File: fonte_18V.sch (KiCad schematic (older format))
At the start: 27 parts, among them U1 LMR16030

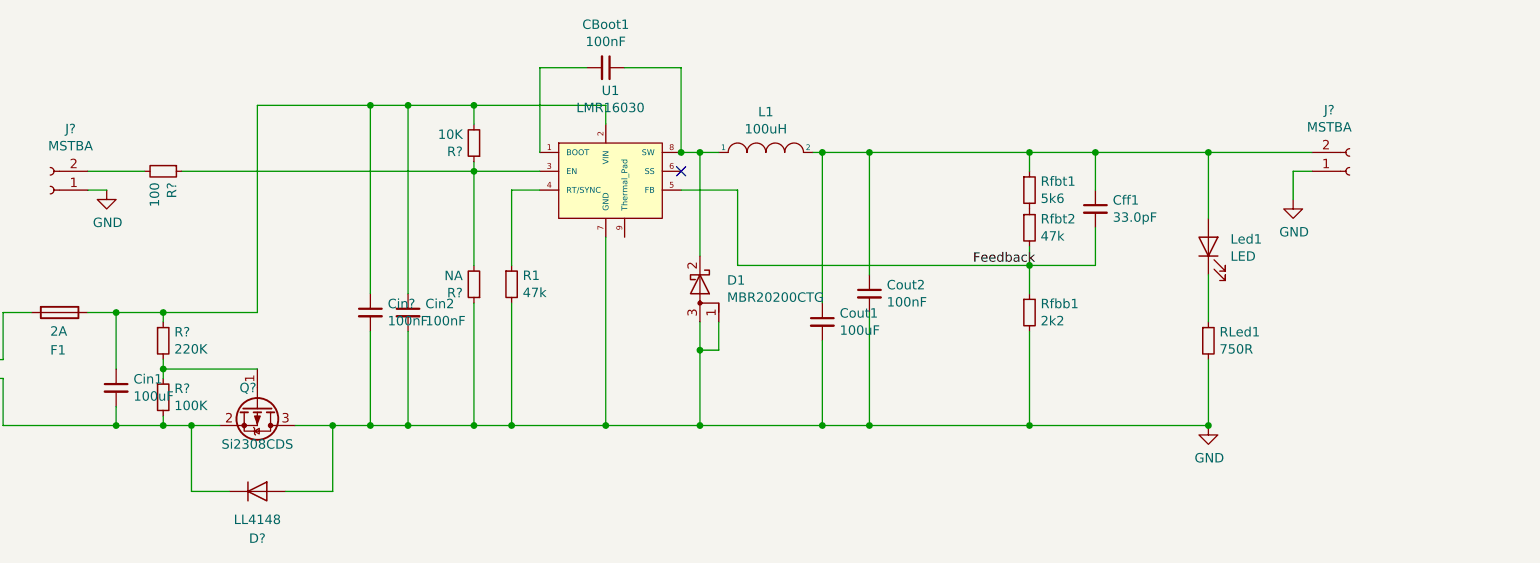
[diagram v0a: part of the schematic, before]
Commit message: snuber e capacitores adicionados. valores de capacitores alterados
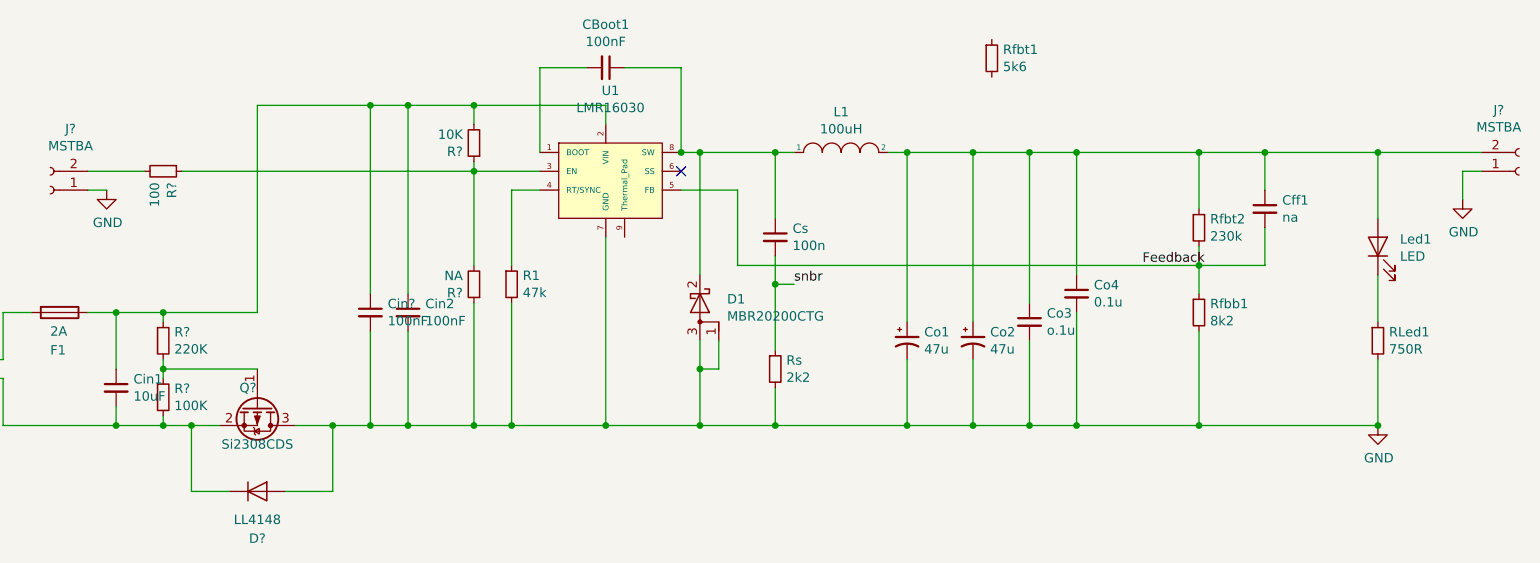
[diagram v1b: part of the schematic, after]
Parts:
- added Co1, Co2: 47u, symbol Device:CP1_Small
- added Cs: 100n, Capacitor_THT:CP_Radial_D8.0mm_P3.80mm, symbol fonte_18V-rescue:C_Small-Device
- added Rs: 2k2, Resistor_SMD:R_0805_2012Metric_Pad1.15x1.40mm_HandSolder, symbol fonte_18V-rescue:R_Small-Device
- Cff1: value 33.0pF -> na
- Cin1: value 100uF -> 10uF
- Co3: renamed from Cout1; value 100uF -> o.1u
- Co4: renamed from Cout2; value 100nF -> 0.1u
- Rfbb1: value 2k2 -> 8k2
- Rfbt2: value 47k -> 230k
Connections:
- net GND: now also Co1.2, Co2.2, Rs.2
- net at CBoot1.1, D1.2 (K), L1.1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: now also Cs.1
- net at Cff1.1, Co3.1, Co4.1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: now also Rfbt2.1, Co1.1, Co2.1; no longer Rfbt1.1
- net at Rfbt1.2: no longer Rfbt2.1
- new net snbr: Cs.2, Rs.1
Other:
- moved on the sheet: Cff1, Co3, Co4, D1, J?, L1, Led1, RLed1, Rfbb1, Rfbt1, Rfbt2

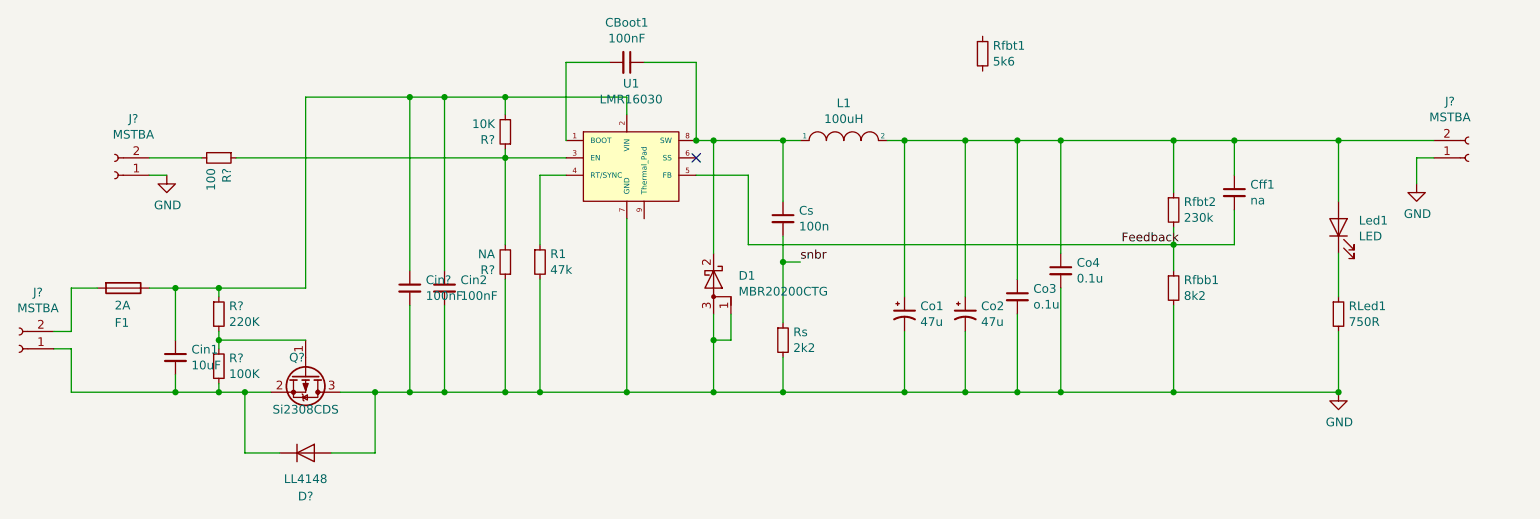
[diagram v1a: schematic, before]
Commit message: mudança de capacitores de entrada nomeou os componentes do circuito footprints alterados erc rodado
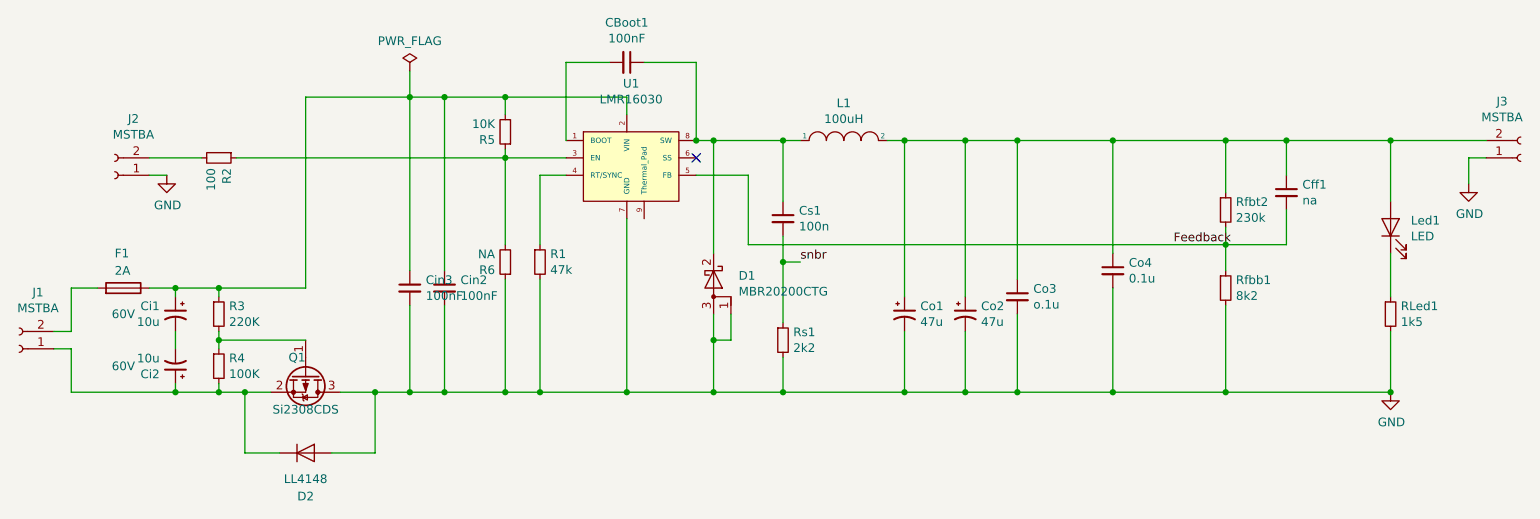
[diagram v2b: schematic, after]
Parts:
- removed Cin1: 10uF, Capacitor_THT:CP_Radial_D8.0mm_P3.80mm, symbol fonte_18V-rescue:C_Small-Device
- removed Rfbt1: 5k6, Resistor_SMD:R_0805_2012Metric_Pad1.15x1.40mm_HandSolder, symbol fonte_18V-rescue:R_Small-Device
- added Ci1, Ci2: 10u, Capacitor_THT:CP_Radial_D5.0mm_P2.50mm, symbol Device:CP1_Small
- Co1, Co2: footprint (none) -> Capacitor_THT:CP_Radial_D5.0mm_P2.50mm
- Co3: footprint Capacitor_THT:CP_Radial_D8.0mm_P3.80mm -> Capacitor_SMD:C_0805_2012Metric_Pad1.15x1.40mm_HandSolder
- Cs1: renamed from Cs; footprint Capacitor_THT:CP_Radial_D8.0mm_P3.80mm -> Capacitor_SMD:C_0805_2012Metric_Pad1.15x1.40mm_HandSolder
- RLed1: value 750R -> 1k5
- gave numbers to parts that had none: 11
- renumbered Rs to Rs1
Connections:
- net at Cin2.1, Cin3.1, F1.1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: now also Ci1.1
- net at D2.1 (K), J1.1 (Pin_1), Q1.2 (S)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: now also Ci2.1
- new net: Ci1.2, Ci2.2
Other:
- moved on the sheet: Cff1, Co4, J3, Led1, RLed1, Rfbb1, Rfbt2

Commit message: Conectores rj45 adicionados, trilhas melhoradas, acabamentos gerais
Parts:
- removed D2: LL4148, Diode_SMD:D_MiniMELF, symbol Diode:LL4148
- removed J3: MSTBA, Connector_Phoenix_MSTB:PhoenixContact_MSTBA_2,5_2-G-5,08_1x02_P5.08mm_Horizontal, symbol Connector:Conn_01x02_Female
- added H1, H2, H3, H4: MountingHole, MountingHole:MountingHole_3.2mm_M3, symbol Mechanical:MountingHole
- added J3, J4: RJ45_Shielded, MFP19RJ45:RJ45_YH59_01, symbol Connector:RJ45_Shielded
- Q1: symbol Transistor_FET:Si2319CDS -> Device:Q_NMOS_GSD
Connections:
- net GND: now also Q1.2 (S), R4.2, U1.9 (Thermal_Pad), J3.3, J3.6, J3.7, J3.8, J3.SH, J4.3, J4.6, J4.7, J4.8, J4.SH; no longer Q1.3 (D)
- net CAN_18V: now reaches Cff1.1, Co1.1, Co2.1, Co3.1, Co4.1, L1.2, Led1.2 (A), Rfbt2.1
- net CAN_18V: now also J3.4, J3.5, J4.4, J4.5
- net at Ci2.1, J1.1 (Pin_1): now also Q1.3 (D); no longer Q1.2 (S), R4.2
- no-connect marks 1 -> 5
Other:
- moved on the sheet: CBoot1, Cff1, Ci1, Ci2, Cin2, Cin3, Co1, Co2, Co3, Co4, Cs1, D1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

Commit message: atualizado
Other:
- moved on the sheet: H1, H2, H3, H4
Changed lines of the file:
@@
 L Mechanical:MountingHole H4
 U 1 1 5DB5A7FD
-P 11550 200
-F 0 "H4" H 11650 246 50  0000 L CNN
-F 1 "MountingHole" H 11650 155 50  0000 L CNN
-F 2 "MountingHole:MountingHole_3.2mm_M3" H 11550 200 50  0001 C CNN
-F 3 "~" H 11550 200 50  0001 C CNN
-	1    11550 200
+P 3250 2200
+F 0 "H4" H 3350 2246 50  0000 L CNN
+F 1 "MountingHole" H 3350 2155 50  0000 L CNN
+F 2 "MountingHole:MountingHole_3.2mm_M3" H 3250 2200 50  0001 C CNN
+F 3 "~" H 3250 2200 50  0001 C CNN
+	1    3250 2200
 	1    0    0    -1
 $EndComp
@@
 L Mechanical:MountingHole H3
 U 1 1 5DB774A1
-P 11500 8100
-F 0 "H3" H 11600 8146 50  0000 L CNN
-F 1 "MountingHole" H 11600 8055 50  0000 L CNN
-F 2 "MountingHole:MountingHole_3.2mm_M3" H 11500 8100 50  0001 C CNN
-F 3 "~" H 11500 8100 50  0001 C CNN
-	1    11500 8100
+P 3250 2550
+F 0 "H3" H 3350 2596 50  0000 L CNN
+F 1 "MountingHole" H 3350 2505 50  0000 L CNN
+F 2 "MountingHole:MountingHole_3.2mm_M3" H 3250 2550 50  0001 C CNN
+F 3 "~" H 3250 2550 50  0001 C CNN
+	1    3250 2550
 	1    0    0    -1
 $EndComp
@@
 L Mechanical:MountingHole H2
 U 1 1 5DB7A851
-P 200 8100
-F 0 "H2" H 300 8146 50  0000 L CNN
-F 1 "MountingHole" H 300 8055 50  0000 L CNN
-F 2 "MountingHole:MountingHole_3.2mm_M3" H 200 8100 50  0001 C CNN
-F 3 "~" H 200 8100 50  0001 C CNN
-	1    200  8100
+P 2350 2550
+F 0 "H2" H 2450 2596 50  0000 L CNN
+F 1 "MountingHole" H 2450 2505 50  0000 L CNN
+F 2 "MountingHole:MountingHole_3.2mm_M3" H 2350 2550 50  0001 C CNN
+F 3 "~" H 2350 2550 50  0001 C CNN
+	1    2350 2550
 	1    0    0    -1
 $EndComp
@@
 L Mechanical:MountingHole H1
 U 1 1 5DB7DBB6
-P 200 150
-F 0 "H1" H 300 196 50  0000 L CNN
-F 1 "MountingHole" H 300 105 50  0000 L CNN
-F 2 "MountingHole:MountingHole_3.2mm_M3" H 200 150 50  0001 C CNN
-F 3 "~" H 200 150 50  0001 C CNN
-	1    200  150
+P 2350 2200
+F 0 "H1" H 2450 2246 50  0000 L CNN
+F 1 "MountingHole" H 2450 2155 50  0000 L CNN
+F 2 "MountingHole:MountingHole_3.2mm_M3" H 2350 2200 50  0001 C CNN
+F 3 "~" H 2350 2200 50  0001 C CNN
+	1    2350 2200
 	1    0    0    -1
 $EndComp
